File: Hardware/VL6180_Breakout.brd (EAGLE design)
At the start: 17.8 x 15.2 mm, 17 parts, among them U1 VL6180

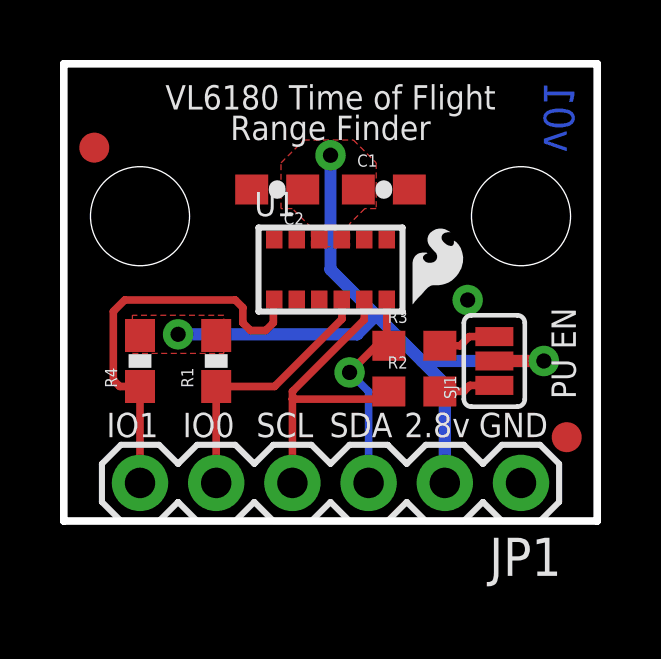
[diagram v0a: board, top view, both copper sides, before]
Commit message: fixed flipped pin problem.  8-9 on the sensor were reversed somehow.  All better :)
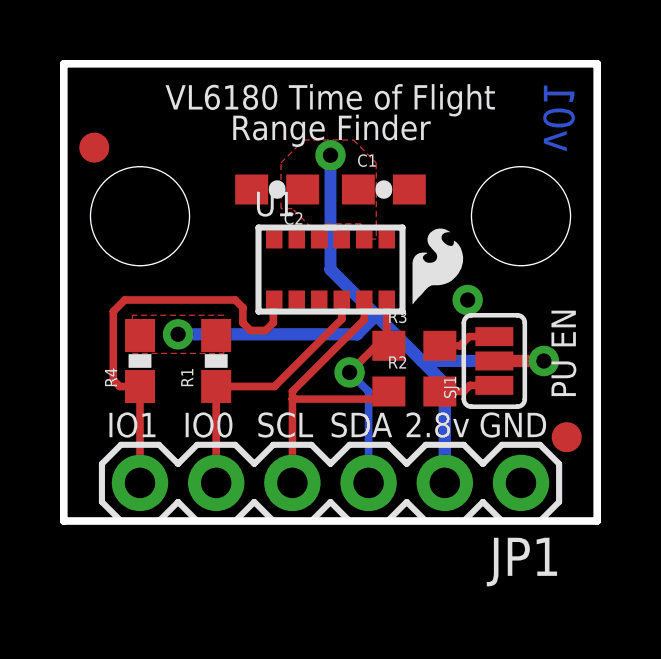
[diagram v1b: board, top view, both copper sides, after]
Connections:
- net 2.8V: now also U1.8; no longer U1.9
- net GND: now also U1.9; no longer U1.8
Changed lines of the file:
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@@
 <setting verticaltext="up"/>
 </settings>
-<grid distance="0.05" unitdist="inch" unit="inch" style="lines" multiple="1" display="yes" altdistance="0.005" altunitdist="inch" altunit="inch"/>
+<grid distance="0.01" unitdist="inch" unit="inch" style="lines" multiple="1" display="yes" altdistance="0.005" altunitdist="inch" altunit="inch"/>
 <layers>
 <layer number="1" name="Top" color="4" fill="1" visible="yes" active="yes"/>
@@
 <layer number="15" name="Route15" color="4" fill="6" visible="no" active="no"/>
 <layer number="16" name="Bottom" color="1" fill="1" visible="no" active="yes"/>
-<layer number="17" name="Pads" color="2" fill="1" visible="yes" active="yes"/>
-<layer number="18" name="Vias" color="2" fill="1" visible="yes" active="yes"/>
-<layer number="19" name="Unrouted" color="6" fill="1" visible="no" active="yes"/>
+<layer number="17" name="Pads" color="2" fill="1" visible="no" active="yes"/>
+<layer number="18" name="Vias" color="2" fill="1" visible="no" active="yes"/>
+<layer number="19" name="Unrouted" color="6" fill="1" visible="yes" active="yes"/>
 <layer number="20" name="Dimension" color="15" fill="1" visible="no" active="yes"/>
-<layer number="21" name="tPlace" color="16" fill="1" visible="yes" active="yes"/>
+<layer number="21" name="tPlace" color="16" fill="1" visible="no" active="yes"/>
 <layer number="22" name="bPlace" color="14" fill="1" visible="no" active="yes"/>
 <layer number="23" name="tOrigins" color="15" fill="1" visible="no" active="yes"/>
@@
 </signal>
 <signal name="GND">
-<contactref element="U1" pad="8"/>
+<contactref element="U1" pad="9"/>
 <contactref element="U1" pad="12"/>
 <contactref element="C2" pad="2"/>
@@
 <contactref element="C2" pad="1"/>
 <contactref element="C1" pad="1"/>
-<contactref element="U1" pad="9"/>
+<contactref element="U1" pad="8"/>
 <contactref element="U1" pad="10"/>
 <contactref element="R4" pad="2"/>
@@
 <vertex x="9.652" y="12.7"/>
 <vertex x="10.414" y="11.938"/>
-<vertex x="10.414" y="10.414"/>
-<vertex x="10.033" y="10.414"/>
-<vertex x="9.525" y="9.906"/>
-<vertex x="9.525" y="9.144"/>
-<vertex x="8.255" y="9.144"/>
+<vertex x="10.414" y="9.398"/>
+<vertex x="9.906" y="9.398"/>
+<vertex x="9.906" y="9.906"/>
+<vertex x="8.763" y="9.906"/>
+<vertex x="8.763" y="9.398"/>
+<vertex x="8.255" y="9.398"/>
 <vertex x="8.255" y="9.779"/>
 <vertex x="7.62" y="10.414"/>

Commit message: added pin 1 designator
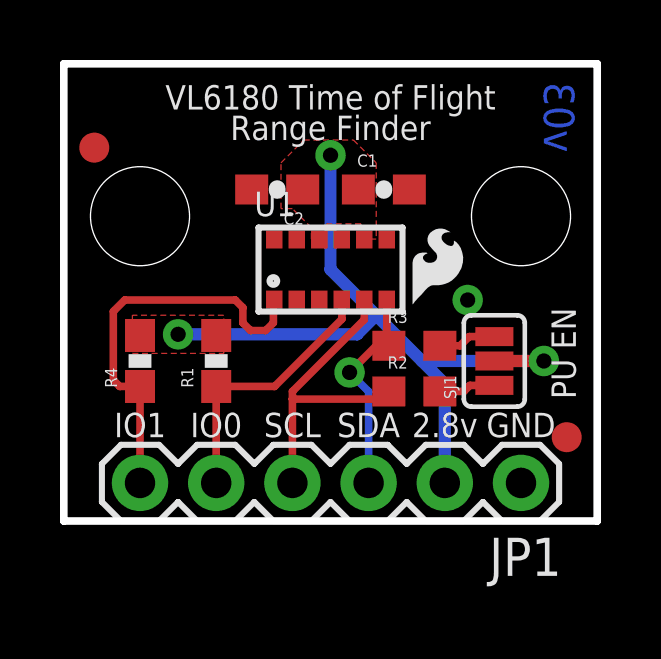
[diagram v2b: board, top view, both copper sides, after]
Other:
- board text added: "v03"
- board text removed: "v01"

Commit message: modified:   Hardware/VL6180_Breakout.brd 	modified:   Hardware/VL6180_Breakout.sch 	renamed:    Hardware/VL6180.brd -> Hardware/VL6180_Sensor.brd 	renamed:    Hardware/VL6180.sch -> Hardware/VL6180_Sensor.sch
Removed I2C level shifter and switched to Fet bases solution.
New solderpaste footprint for VL6180 for improved reflow.
updated all parts with Sparkle ID's
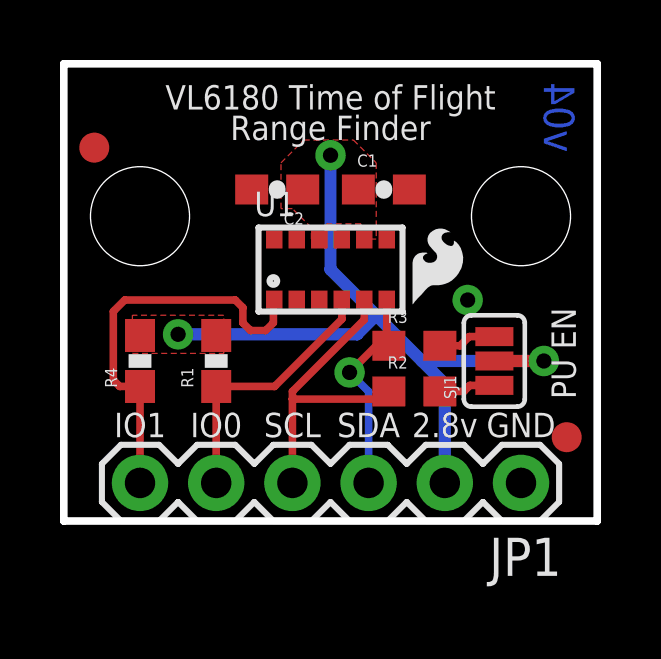
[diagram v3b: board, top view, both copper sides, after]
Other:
- board text added: "v04"
- board text removed: "v03"
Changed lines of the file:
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@@
 <grid distance="0.01" unitdist="inch" unit="inch" style="lines" multiple="1" display="yes" altdistance="0.005" altunitdist="inch" altunit="inch"/>
 <layers>
-<layer number="1" name="Top" color="4" fill="1" visible="no" active="yes"/>
+<layer number="1" name="Top" color="4" fill="1" visible="yes" active="yes"/>
 <layer number="2" name="Route2" color="1" fill="3" visible="no" active="no"/>
 <layer number="3" name="Route3" color="4" fill="3" visible="no" active="no"/>
@@
 <layer number="19" name="Unrouted" color="6" fill="1" visible="yes" active="yes"/>
 <layer number="20" name="Dimension" color="15" fill="1" visible="yes" active="yes"/>
-<layer number="21" name="tPlace" color="16" fill="1" visible="no" active="yes"/>
+<layer number="21" name="tPlace" color="16" fill="1" visible="yes" active="yes"/>
 <layer number="22" name="bPlace" color="14" fill="1" visible="yes" active="yes"/>
-<layer number="23" name="tOrigins" color="15" fill="1" visible="no" active="yes"/>
-<layer number="24" name="bOrigins" color="15" fill="1" visible="no" active="yes"/>
-<layer number="25" name="tNames" color="7" fill="1" visible="no" active="yes"/>
-<layer number="26" name="bNames" color="7" fill="1" visible="no" active="yes"/>
-<layer number="27" name="tValues" color="7" fill="1" visible="no" active="yes"/>
-<layer number="28" name="bValues" color="7" fill="1" visible="no" active="yes"/>
-<layer number="29" name="tStop" color="7" fill="3" visible="no" active="yes"/>
-<layer number="30" name="bStop" color="7" fill="6" visible="no" active="yes"/>
-<layer number="31" name="tCream" color="7" fill="4" visible="no" active="yes"/>
-<layer number="32" name="bCream" color="7" fill="5" visible="no" active="yes"/>
+<layer number="23" name="tOrigins" color="15" fill="1" visible="yes" active="yes"/>
+<layer number="24" name="bOrigins" color="15" fill="1" visible="yes" active="yes"/>
+<layer number="25" name="tNames" color="7" fill="1" visible="yes" active="yes"/>
+<layer number="26" name="bNames" color="7" fill="1" visible="yes" active="yes"/>
+<layer number="27" name="tValues" color="7" fill="1" visible="yes" active="yes"/>
+<layer number="28" name="bValues" color="7" fill="1" visible="yes" active="yes"/>
+<layer number="29" name="tStop" color="7" fill="3" visible="yes" active="yes"/>
+<layer number="30" name="bStop" color="7" fill="6" visible="yes" active="yes"/>
+<layer number="31" name="tCream" color="7" fill="4" visible="yes" active="yes"/>
+<layer number="32" name="bCream" color="7" fill="5" visible="yes" active="yes"/>
 <layer number="33" name="tFinish" color="6" fill="3" visible="yes" active="yes"/>
 <layer number="34" name="bFinish" color="6" fill="6" visible="yes" active="yes"/>
@@
 <layer number="44" name="Drills" color="7" fill="1" visible="yes" active="yes"/>
 <layer number="45" name="Holes" color="7" fill="1" visible="yes" active="yes"/>
-<layer number="46" name="Milling" color="3" fill="1" visible="no" active="yes"/>
-<layer number="47" name="Measures" color="7" fill="1" visible="no" active="yes"/>
+<layer number="46" name="Milling" color="3" fill="1" visible="yes" active="yes"/>
+<layer number="47" name="Measures" color="7" fill="1" visible="yes" active="yes"/>
 <layer number="48" name="Document" color="7" fill="1" visible="yes" active="yes"/>
-<layer number="49" name="Reference" color="7" fill="1" visible="no" active="yes"/>
+<layer number="49" name="Reference" color="7" fill="1" visible="yes" active="yes"/>
 <layer number="50" name="dxf" color="7" fill="1" visible="no" active="no"/>
-<layer number="51" name="tDocu" color="6" fill="1" visible="no" active="yes"/>
-<layer number="52" name="bDocu" color="7" fill="1" visible="no" active="yes"/>
+<layer number="51" name="tDocu" color="6" fill="1" visible="yes" active="yes"/>
+<layer number="52" name="bDocu" color="7" fill="1" visible="yes" active="yes"/>
 <layer number="53" name="tGND_GNDA" color="7" fill="9" visible="no" active="no"/>
 <layer number="54" name="bGND_GNDA" color="1" fill="9" visible="no" active="no"/>
@@
 <plain>
 <text x="26.5" y="-9.5" size="1.778" layer="51">Casey Kuhns</text>
-<text x="17.018" y="13.462" size="1.016" layer="16" font="vector" ratio="20" rot="MR270" align="bottom-center">v03</text>
+<text x="17.018" y="13.462" size="1.016" layer="16" font="vector" ratio="20" rot="MR270" align="bottom-center">v04</text>
 <text x="15.24" y="2.794" size="0.8128" layer="21" font="vector" ratio="15" align="bottom-center">GND</text>
 <text x="12.7" y="2.794" size="0.8128" layer="21" font="vector" ratio="15" align="bottom-center">2.8v</text>
@@
 <elements>
 <element name="FRAME1" library="SparkFun-Aesthetics" package="CREATIVE_COMMONS" value="FRAME-LETTER" x="0" y="-9.5"/>
-<element name="U1" library="VL6180" package="VL6180" value="VL6180" x="8.89" y="8.382"/>
+<element name="U1" library="VL6180" package="VL6180" value="VL6180" x="8.89" y="8.382">
+<attribute name="PROD_ID" value="IC-12007" x="8.89" y="8.382" size="1.778" layer="27" display="off"/>
+</element>
 <element name="R2" library="SparkFun-Resistors" package="0603" value="4.7k" x="11.684" y="4.318">
 <attribute name="PROD_ID" value="RES-07857" x="11.684" y="4.318" size="1.778" layer="27" display="off"/>

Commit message: changed I2C resistors to 2.2k, added current limiting resistor on GPIO pins.
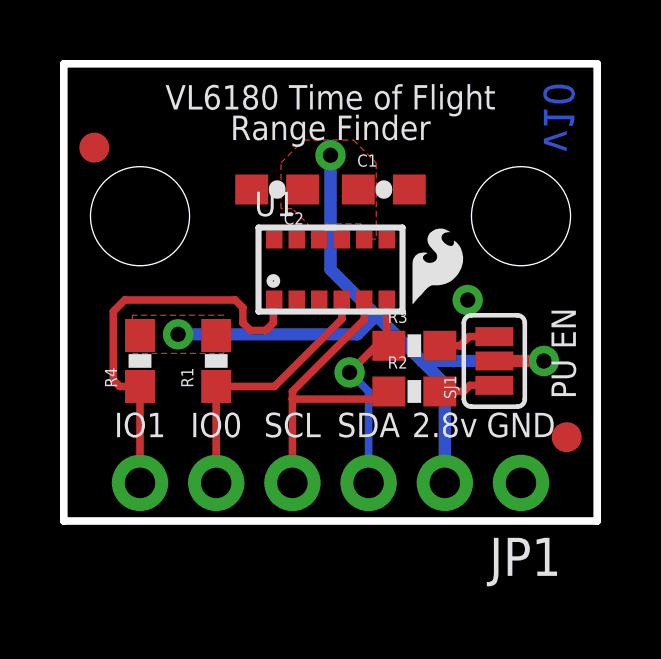
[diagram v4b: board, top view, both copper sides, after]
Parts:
- R1, R4: value 10K -> 47K
- R2, R3: value 4.7k -> 2.2k; device SparkFun-Resistors:0603 -> SparkFun-Resistors:0603-RES
- SJ1: device SparkFun-Passives:SJ_3_PASTE1&2&3 -> SparkFun-Passives:PAD-JUMPER-3-NC_BY_PASTE_YES_SILK_FULL_BOX
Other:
- board text added: "v10"
- board text removed: "v04"
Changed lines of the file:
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@@
 <layer number="54" name="bGND_GNDA" color="1" fill="9" visible="no" active="no"/>
 <layer number="56" name="wert" color="7" fill="1" visible="no" active="no"/>
+<layer number="57" name="tCAD" color="7" fill="1" visible="no" active="no"/>
 <layer number="91" name="Nets" color="2" fill="1" visible="no" active="no"/>
 <layer number="92" name="Busses" color="1" fill="1" visible="no" active="no"/>
@@
 <layer number="97" name="Info" color="7" fill="1" visible="no" active="no"/>
 <layer number="98" name="Guide" color="6" fill="1" visible="no" active="no"/>
+<layer number="99" name="SpiceOrder" color="7" fill="1" visible="no" active="no"/>
 <layer number="100" name="Muster" color="7" fill="1" visible="no" active="no"/>
 <layer number="101" name="Patch_Top" color="12" fill="4" visible="yes" active="yes"/>
@@
 <layer number="108" name="tplace-old" color="10" fill="1" visible="yes" active="yes"/>
 <layer number="109" name="ref-old" color="11" fill="1" visible="yes" active="yes"/>
+<layer number="110" name="fp0" color="7" fill="1" visible="yes" active="yes"/>
+<layer number="111" name="LPC17xx" color="7" fill="1" visible="yes" active="yes"/>
+<layer number="112" name="tSilk" color="7" fill="1" visible="yes" active="yes"/>
+<layer number="113" name="IDFDebug" color="4" fill="1" visible="yes" active="yes"/>
 <layer number="116" name="Patch_BOT" color="9" fill="4" visible="yes" active="yes"/>
 <layer number="121" name="_tsilk" color="7" fill="1" visible="yes" active="yes"/>
 <layer number="122" name="_bsilk" color="7" fill="1" visible="yes" active="yes"/>
+<layer number="123" name="tTestmark" color="7" fill="1" visible="yes" active="yes"/>
+<layer number="124" name="bTestmark" color="7" fill="1" visible="yes" active="yes"/>
 <layer number="125" name="_tNames" color="7" fill="1" visible="yes" active="yes"/>
+<layer number="126" name="_bNames" color="7" fill="1" visible="yes" active="yes"/>
+<layer number="127" name="_tValues" color="7" fill="1" visible="yes" active="yes"/>
+<layer number="128" name="_bValues" color="7" fill="1" visible="yes" active="yes"/>
+<layer number="131" name="tAdjust" color="7" fill="1" visible="yes" active="yes"/>
+<layer number="132" name="bAdjust" color="7" fill="1" visible="yes" active="yes"/>
 <layer number="144" name="Drill_legend" color="7" fill="1" visible="yes" active="yes"/>
+<layer number="150" name="Notes" color="7" fill="1" visible="yes" active="yes"/>
 <layer number="151" name="HeatSink" color="7" fill="1" visible="yes" active="yes"/>
+<layer number="152" name="_bDocu" color="7" fill="1" visible="yes" active="yes"/>
+<layer number="153" name="FabDoc1" color="7" fill="1" visible="yes" active="yes"/>
+<layer number="154" name="FabDoc2" color="7" fill="1" visible="yes" active="yes"/>
+<layer number="155" name="FabDoc3" color="7" fill="1" visible="yes" active="yes"/>
 <layer number="199" name="Contour" color="7" fill="1" visible="yes" active="yes"/>
 <layer number="200" name="200bmp" color="1" fill="10" visible="yes" active="yes"/>
@@
 <layer number="223" name="223bmp" color="24" fill="1" visible="no" active="no"/>
 <layer number="224" name="224bmp" color="25" fill="1" visible="no" active="no"/>
+<layer number="248" name="Housing" color="7" fill="1" visible="yes" active="yes"/>
+<layer number="249" name="Edge" color="7" fill="1" visible="yes" active="yes"/>
 <layer number="250" name="Descript" color="3" fill="1" visible="no" active="no"/>
 <layer number="251" name="SMDround" color="12" fill="11" visible="no" active="no"/>
@@
 <plain>
 <text x="26.5" y="-9.5" size="1.778" layer="51">Casey Kuhns</text>
-<text x="17.018" y="13.462" size="1.016" layer="16" font="vector" ratio="20" rot="MR270" align="bottom-center">v04</text>
+<text x="17.018" y="13.462" size="1.016" layer="16" font="vector" ratio="20" rot="MR270" align="bottom-center">v10</text>
 <text x="15.24" y="2.794" size="0.8128" layer="21" font="vector" ratio="15" align="bottom-center">GND</text>
 <text x="12.7" y="2.794" size="0.8128" layer="21" font="vector" ratio="15" align="bottom-center">2.8v</text>
@@
 <attribute name="PROD_ID" value="IC-12007" x="8.89" y="8.382" size="1.778" layer="27" display="off"/>
 </element>
-<element name="R2" library="SparkFun-Resistors" package="0603" value="4.7k" x="11.684" y="4.318">
-<attribute name="PROD_ID" value="RES-07857" x="11.684" y="4.318" size="1.778" layer="27" display="off"/>
-</element>
-<element name="R3" library="SparkFun-Resistors" package="0603" value="4.7k" x="11.684" y="5.842">
-<attribute name="PROD_ID" value="RES-07857" x="11.684" y="5.842" size="1.778" layer="27" display="off"/>
-</element>
-<element name="R4" library="SparkFun-Resistors" package="0603-RES" value="10K" x="2.54" y="5.334" rot="R90">
-<attribute name="PROD_ID" value="RES-00824" x="2.54" y="5.334" size="1.778" layer="27" rot="R90" display="off"/>
+<element name="R2" library="SparkFun-Resistors" package="0603-RES" value="2.2k" x="11.684" y="4.318">
+<attribute name="PROD_ID" value="RES-08272" x="11.684" y="4.318" size="1.778" layer="27" display="off"/>
+<attribute name="VALUE" value="2.2k" x="11.684" y="4.318" size="1.778" layer="27" display="off"/>
+</element>
+<element name="R3" library="SparkFun-Resistors" package="0603-RES" value="2.2k" x="11.684" y="5.842">
+<attribute name="PROD_ID" value="RES-08272" x="11.684" y="5.842" size="1.778" layer="27" display="off"/>
+<attribute name="VALUE" value="2.2k" x="11.684" y="5.842" size="1.778" layer="27" display="off"/>
+</element>
+<element name="R4" library="SparkFun-Resistors" package="0603-RES" value="47K" x="2.54" y="5.334" rot="R90">
+<attribute name="PROD_ID" value="RES-07871" x="2.54" y="5.334" size="1.778" layer="27" rot="R90" display="off"/>
 </element>
 <element name="C1" library="SparkFun-Capacitors" package="0603-CAP" value="4.7uF" x="10.668" y="11.049">
@@
 <element name="STANDOFF2" library="SparkFun-Electromechanical" package="STAND-OFF" value="STAND-OFF" x="15.24" y="10.16"/>
 <element name="JP1" library="SparkFun-Connectors" package="1X06" value="" x="15.24" y="1.27" rot="R180"/>
-<element name="R1" library="SparkFun-Resistors" package="0603-RES" value="10K" x="5.08" y="5.334" rot="R90">
-<attribute name="PROD_ID" value="RES-00824" x="5.08" y="5.334" size="1.778" layer="27" rot="R90" display="off"/>
+<element name="R1" library="SparkFun-Resistors" package="0603-RES" value="47K" x="5.08" y="5.334" rot="R90">
+<attribute name="PROD_ID" value="RES-07871" x="5.08" y="5.334" size="1.778" layer="27" rot="R90" display="off"/>
 </element>
 <element name="U$2" library="SparkFun-Aesthetics" package="SFE_LOGO_FLAME_.1" value="" x="11.303" y="6.858"/>
@@
 <element name="FID1" library="SparkFun-Aesthetics" package="FIDUCIAL-1X2" value="FIDUCIAL1X2" x="16.764" y="2.794"/>
 <element name="FID2" library="SparkFun-Aesthetics" package="FIDUCIAL-1X2" value="FIDUCIAL1X2" x="1.016" y="12.446"/>
-<element name="SJ1" library="SparkFun-Passives" package="SJ_3_PASTE1&amp;2&amp;3" value="" x="14.351" y="5.334" rot="R90"/>
+<element name="SJ1" library="SparkFun-Passives" package="PAD-JUMPER-3-NC_BY_PASTE_YES_SILK_FULL_BOX" value="" x="14.351" y="5.334" rot="R90"/>
 </elements>
 <signals>
